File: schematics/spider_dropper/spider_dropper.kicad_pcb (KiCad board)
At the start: 2 copper layers, 80 x 20 mm, 10 parts, among them J1 JST_XH_3, J2 PJ-044AH, J3 JST_XH_2, Q1 IRLZ34N, SW1 ZX40E20C01

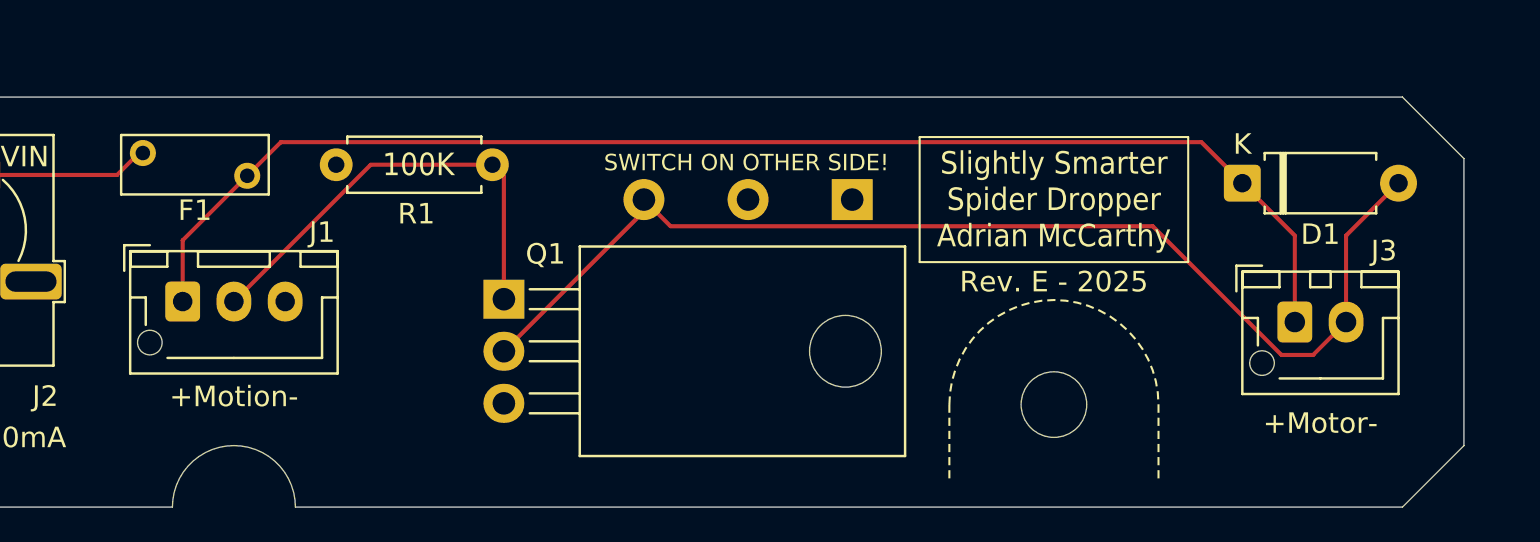
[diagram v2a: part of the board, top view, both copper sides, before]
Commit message: Small improvements for Rev. E.
* Moved the connectors to make it easier to connect & disconnect.
* Moved the diode in from the corner.
* Added detail to the perimeter boundary (in User Drawings layer).
* Added a triangular arrow to assist with alignment in assembly.
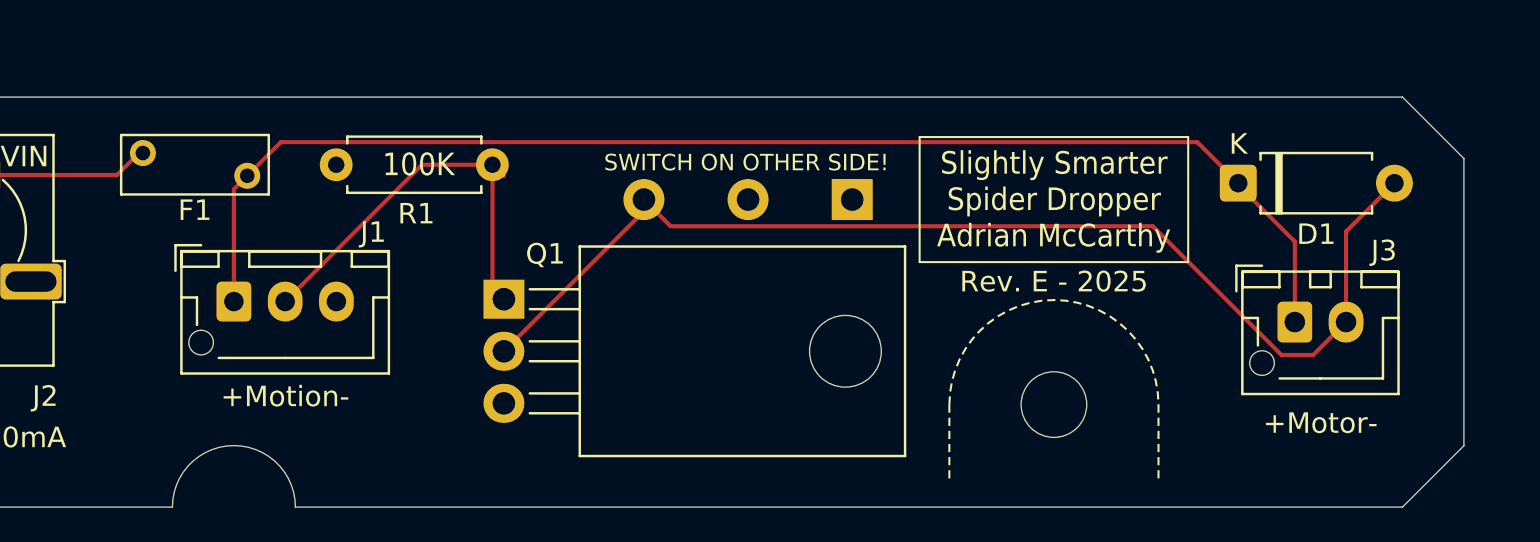
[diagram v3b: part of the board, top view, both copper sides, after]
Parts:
- moved J1 2.50 mm to (129.9, 108.3)
- moved D1 0.20 mm to (178.9, 102.5)
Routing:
- net /MOTION: track 22.2 -> 20.5 mm
- net /MOTOR+: track 65.3 -> 64.2 mm
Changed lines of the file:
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@@
 	(title_block
 		(title "Slightly Smarter Simple Spider Dropper")
-		(date "2025-08-28")
+		(date "2025-09-18")
 		(rev "E")
 		(company "Adrian McCarthy")
@@
 		(comment 6 "corrected footprint for power connector")
 		(comment 7 "nudged diode away from corner")
+		(comment 8 "added arrow on b. silkscreen")
 	)
 	(layers
@@
 	(footprint "Diode_THT:D_A-405_P7.62mm_Horizontal"
 		(layer "F.Cu")
-		(at 179.09 102.5)
+		(at 178.89 102.5)
 		(descr "Diode, A-405 series, Axial, Horizontal, pin pitch=7.62mm, length*diameter=5.2*2.7mm^2, http://www.diodes.com/_files/packages/A-405.pdf")
 		(tags "Diode A-405 series Axial Horizontal pin pitch 7.62mm  length 5.2mm diameter 2.7mm")
@@
 	(footprint "Connector_JST:JST_XH_B3B-XH-AM_1x03_P2.50mm_Vertical"
 		(layer "F.Cu")
-		(at 127.4 108.275)
+		(at 129.9 108.275)
 		(descr "JST XH series connector, B3B-XH-AM, with boss (http://www.jst-mfg.com/product/pdf/eng/eXH.pdf), generated with kicad-footprint-generator")
 		(tags "connector JST XH vertical boss")
@@
 		(layer "F.SilkS")
 	)
+	(gr_poly
+		(pts
+			(xy 111.2 108.3) (xy 113 107.4) (xy 113 109.2)
+		)
+		(stroke
+			(width 0.1)
+			(type solid)
+		)
+		(fill yes)
+		(layer "B.SilkS")
+	)
 	(gr_circle
 		(center 169.9 113.3)
@@
 		(layer "Dwgs.User")
 	)
+	(gr_arc
+		(start 125.8 117.1)
+		(mid 129.9 114.027998)
+		(end 134 117.1)
+		(stroke
+			(width 0.1)
+			(type default)
+		)
+		(layer "Dwgs.User")
+	)
+	(gr_line
+		(start 188.7 114.8)
+		(end 186.4 117.1)
+		(stroke
+			(width 0.1)
+			(type default)
+		)
+		(layer "Dwgs.User")
+	)
+	(gr_line
+		(start 125.8 117.1)
+		(end 111.1 117.1)
+		(stroke
+			(width 0.1)
+			(type default)
+		)
+		(layer "Dwgs.User")
+	)
 	(gr_line
 		(start 215.7 108.3)
@@
 	)
 	(gr_line
+		(start 186.4 99.5)
+		(end 188.7 101.8)
+		(stroke
+			(width 0.1)
+			(type default)
+		)
+		(layer "Dwgs.User")
+	)
+	(gr_line
+		(start 186.4 117.1)
+		(end 133.999999 117.1)
+		(stroke
+			(width 0.1)
+			(type default)
+		)
+		(layer "Dwgs.User")
+	)
+	(gr_line
 		(start 149.9 97.8)
 		(end 149.9 105.8)
@@
 		(layer "Dwgs.User")
 	)
-	(gr_rect
+	(gr_line
+		(start 188.7 101.8)
+		(end 188.7 114.8)
+		(stroke
+			(width 0.1)
+			(type default)
+		)
+		(layer "Dwgs.User")
+	)
+	(gr_line
 		(start 111.1 99.5)
-		(end 188.7 117.1)
+		(end 186.4 99.5)
+		(stroke
+			(width 0.1)
+			(type default)
+		)
+		(layer "Dwgs.User")
+	)
+	(gr_line
+		(start 111.1 117.1)
+		(end 111.1 99.5)
 		(stroke
 			(width 0.1)
 			(type default)
 		)
-		(fill no)
 		(layer "Dwgs.User")
 	)
@@
 	)
 	(gr_text "+Motion-"
-		(at 129.9 113.5 0)
+		(at 132.4 113.5 0)
 		(layer "F.SilkS")
 		(effects
@@
 	)
 	(segment
-		(start 127.4 108.275)
-		(end 127.4 105.29)
+		(start 178.89 102.59)
+		(end 181.65 105.35)
 		(width 0.2)
 		(layer "F.Cu")
@@
 	)
 	(segment
-		(start 181.65 105.06)
-		(end 179.09 102.5)
+		(start 181.65 105.35)
+		(end 181.65 109.275)
 		(width 0.2)
 		(layer "F.Cu")
@@
 	)
 	(segment
-		(start 181.65 109.275)
-		(end 181.65 105.06)
+		(start 132.191 100.499)
+		(end 176.889 100.499)
 		(width 0.2)
 		(layer "F.Cu")
@@
 	)
 	(segment
-		(start 177.089 100.499)
+		(start 130.55 102.14)
 		(end 132.191 100.499)
 		(width 0.2)
@@
 	)
 	(segment
-		(start 179.09 102.5)
-		(end 177.089 100.499)
+		(start 178.89 102.5)
+		(end 178.89 102.59)
 		(width 0.2)
 		(layer "F.Cu")
@@
 	)
 	(segment
-		(start 127.4 105.29)
-		(end 130.55 102.14)
+		(start 129.9 108.275)
+		(end 129.9 102.79)
 		(width 0.2)
 		(layer "F.Cu")
@@
 	)
 	(segment
-		(start 132.191 100.499)
+		(start 129.9 102.79)
 		(end 130.55 102.14)
 		(width 0.2)
@@
 	)
 	(segment
-		(start 186.71 102.5)
-		(end 184.15 105.06)
+		(start 176.889 100.499)
+		(end 178.89 102.5)
 		(width 0.2)
 		(layer "F.Cu")
-		(net 5)
+		(net 4)
 	)
 	(segment
@@
 	)
 	(segment
-		(start 184.15 105.06)
+		(start 184.15 104.86)
 		(end 184.15 109.275)
 		(width 0.2)
@@
 	)
 	(segment
-		(start 136.575 101.6)
-		(end 142.51 101.6)
+		(start 186.51 102.5)
+		(end 184.15 104.86)
+		(width 0.2)
+		(layer "F.Cu")
+		(net 5)
+	)
+	(segment
+		(start 132.4 108.275)
+		(end 139.075 101.6)
 		(width 0.2)
 		(layer "F.Cu")
@@
 	)
 	(segment
-		(start 143.07 108.16)
-		(end 143.07 102.16)
+		(start 142.51 107.6)
+		(end 143.07 108.16)
+		(width 0.2)
+		(layer "F.Cu")
+		(net 6)
+	)
+	(segment
+		(start 139.075 101.6)
+		(end 142.51 101.6)
 		(width 0.2)
 		(layer "F.Cu")
@@
 	)
 	(segment
-		(start 129.9 108.275)
-		(end 136.575 101.6)
+		(start 142.51 101.6)
+		(end 142.51 107.6)
 		(width 0.2)
 		(layer "F.Cu")
@@
 		)
 	)
+	(group ""
+		(members "1a110cda-c5c4-4d6f-9856-7c3907b5bba1" "1ba40044-9f59-4987-8364-2ef93bba9d79"
+			"79ad52df-f96e-4c85-854d-0dd0dc49f08a" "cd2ad88d-1473-40dd-a4fc-b80dc6a883e4"
+			"d2219a55-52e0-4438-a1ba-f4ec083b581e" "e5993648-c71e-4bc1-9e7f-92ee8b79d6de"
+			"fc64db34-372b-49d4-b4d6-4ea789881956" "fe8aa7d5-6fb3-46ed-a818-365fcd90bb6e"
+		)
+	)

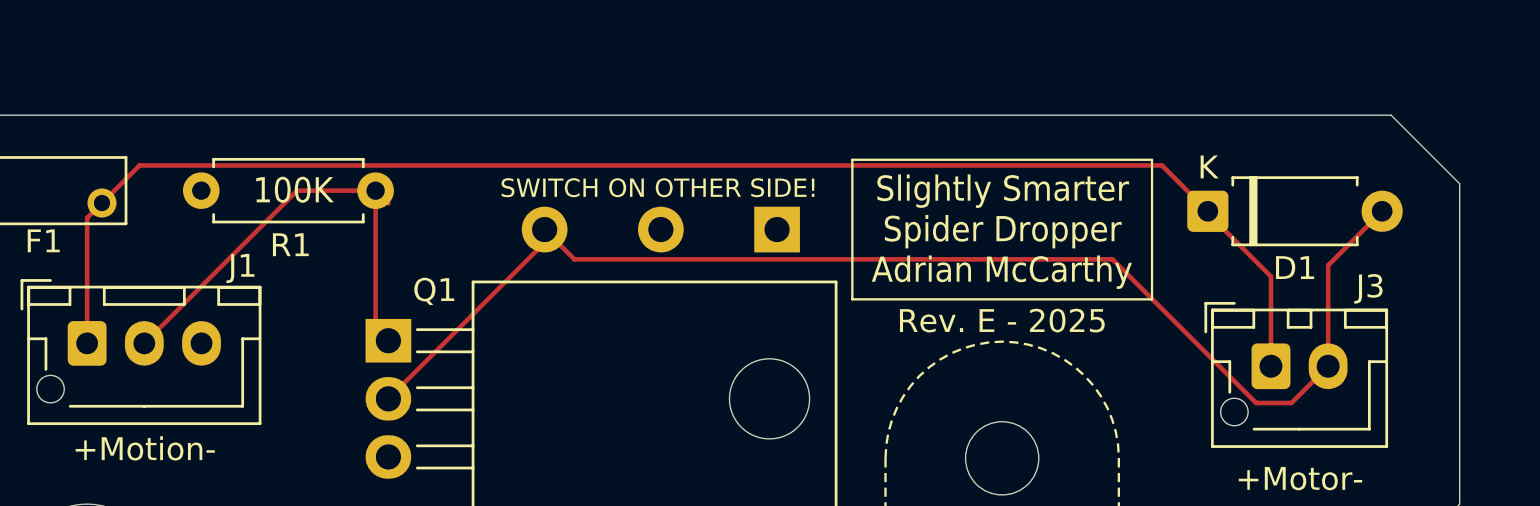
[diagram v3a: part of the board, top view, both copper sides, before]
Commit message: Changed the diode footprint to a DO-41.
The leads of the 1N4001 diodes I have barely fit into the holes for the
default footprint.  Datasheet suggests DO-41 is the correct package,
and KiCad has a footprint for that with the same spacing but larger
holes.
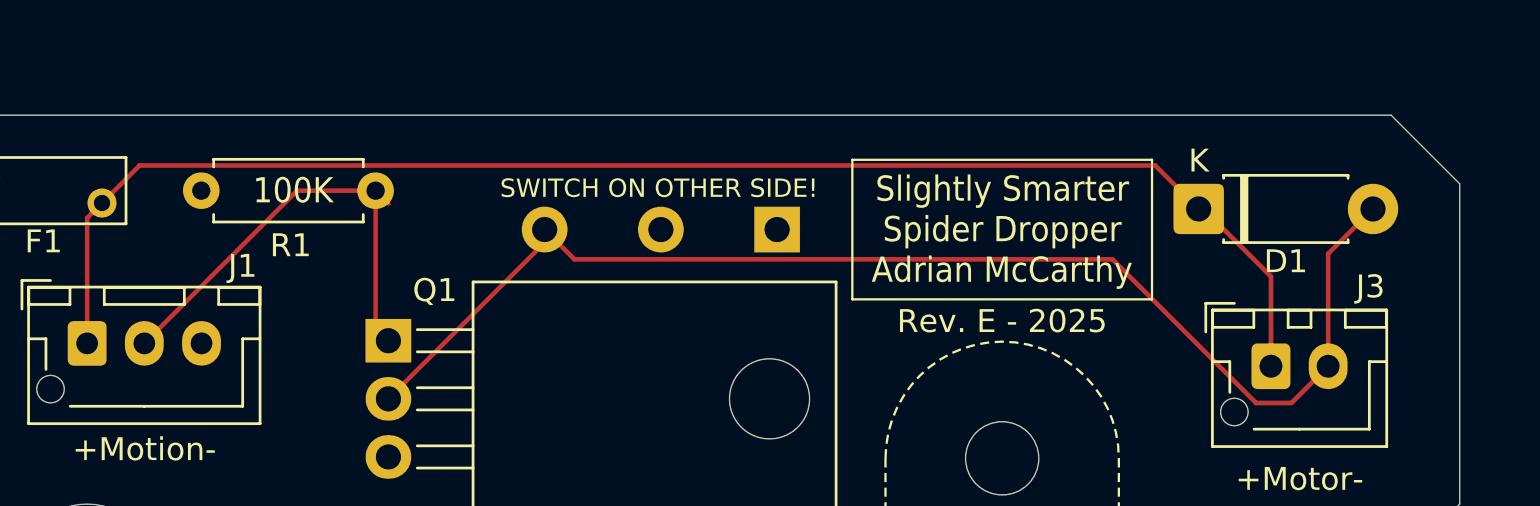
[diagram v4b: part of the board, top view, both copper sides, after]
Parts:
- D1: footprint Diode_THT:D_A-405_P7.62mm_Horizontal -> Diode_THT:D_DO-41_SOD81_P7.62mm_Horizontal
- moved D1 0.41 mm to (178.5, 102.4)
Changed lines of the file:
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@@
 	(title_block
 		(title "Slightly Smarter Simple Spider Dropper")
-		(date "2025-09-18")
+		(date "2025-09-21")
 		(rev "E")
 		(company "Adrian McCarthy")
@@
 	(net 6 "/MOTION")
 	(net 7 "unconnected-(J2-Pad3)")
-	(footprint "Diode_THT:D_A-405_P7.62mm_Horizontal"
+	(footprint "Diode_THT:D_DO-41_SOD81_P7.62mm_Horizontal"
 		(layer "F.Cu")
-		(at 178.89 102.5)
-		(descr "Diode, A-405 series, Axial, Horizontal, pin pitch=7.62mm, length*diameter=5.2*2.7mm^2, http://www.diodes.com/_files/packages/A-405.pdf")
-		(tags "Diode A-405 series Axial Horizontal pin pitch 7.62mm  length 5.2mm diameter 2.7mm")
+		(at 178.49 102.4)
+		(descr "Diode, DO-41_SOD81 series, Axial, Horizontal, pin pitch=7.62mm, length*diameter=5.2*2.7mm^2, https://www.diodes.com/assets/Package-Files/DO-41-Plastic.pdf")
+		(tags "Diode DO-41_SOD81 series Axial Horizontal pin pitch 7.62mm  length 5.2mm diameter 2.7mm")
 		(property "Reference" "D1"
-			(at 3.81 2.5 0)
+			(at 3.81 2.3 0)
 			(layer "F.SilkS")
 			(effects
@@
 		(property "Datasheet" "~"
 			(at 0 0 0)
-			(unlocked yes)
 			(layer "F.Fab")
 			(hide yes)
@@
 		(property "Description" "Diode"
 			(at 0 0 0)
-			(unlocked yes)
 			(layer "F.Fab")
 			(hide yes)
@@
 		)
 		(fp_line
-			(start 1.09 -1.14)
+			(start 1.09 -1.34)
 			(end 1.09 -1.47)
 			(stroke
@@
 		)
 		(fp_line
-			(start 1.09 1.14)
+			(start 1.09 1.34)
 			(end 1.09 1.47)
 			(stroke
@@
 		(fp_line
 			(start 6.53 -1.47)
-			(end 6.53 -1.14)
+			(end 6.53 -1.34)
 			(stroke
 				(width 0.12)
@@
 		(fp_line
 			(start 6.53 1.47)
-			(end 6.53 1.14)
+			(end 6.53 1.34)
 			(stroke
 				(width 0.12)
@@
 		)
 		(fp_rect
-			(start -1.15 -1.6)
-			(end 8.77 1.6)
+			(start -1.35 -1.6)
+			(end 8.97 1.6)
 			(stroke
 				(width 0.05)
@@
 		)
 		(fp_text user "K"
-			(at 0 -1.9 0)
+			(at 0 -2.1 0)
 			(layer "F.SilkS")
 			(effects
@@
 		)
 		(fp_text user "K"
-			(at 0 -1.9 0)
+			(at 0 -2.1 0)
 			(layer "F.Fab")
 			(effects
@@
 		(pad "1" thru_hole roundrect
 			(at 0 0)
-			(size 1.8 1.8)
-			(drill 0.9)
+			(size 2.2 2.2)
+			(drill 1.1)
 			(layers "*.Cu" "*.Mask")
 			(remove_unused_layers no)
-			(roundrect_rratio 0.138889)
+			(roundrect_rratio 0.113636)
 			(net 4 "/MOTOR+")
 			(pinfunction "K")
@@
 		(pad "2" thru_hole circle
 			(at 7.62 0)
-			(size 1.8 1.8)
-			(drill 0.9)
+			(size 2.2 2.2)
+			(drill 1.1)
 			(layers "*.Cu" "*.Mask")
 			(remove_unused_layers no)
@@
 		)
 		(embedded_fonts no)
-		(model "${KICAD9_3DMODEL_DIR}/Diode_THT.3dshapes/D_A-405_P7.62mm_Horizontal.step"
+		(model "${KICAD9_3DMODEL_DIR}/Diode_THT.3dshapes/D_DO-41_SOD81_P7.62mm_Horizontal.step"
 			(offset
 				(xyz 0 0 0)
@@
 	)
 	(segment
-		(start 178.89 102.59)
-		(end 181.65 105.35)
+		(start 132.191 100.499)
+		(end 176.589 100.499)
 		(width 0.2)
 		(layer "F.Cu")
@@
 	)
 	(segment
-		(start 132.191 100.499)
-		(end 176.889 100.499)
+		(start 181.65 105.35)
+		(end 178.7 102.4)
+		(width 0.2)
+		(layer "F.Cu")
+		(net 4)
+	)
+	(segment
+		(start 178.7 102.4)
+		(end 178.49 102.4)
 		(width 0.2)
 		(layer "F.Cu")
@@
 	)
 	(segment
-		(start 176.889 100.499)
-		(end 178.89 102.5)
+		(start 176.589 100.499)
+		(end 178.49 102.4)
 		(width 0.2)
 		(layer "F.Cu")
@@
 	)
 	(segment
-		(start 184.15 104.86)
-		(end 184.15 109.275)
+		(start 184.15 104.36)
+		(end 186.11 102.4)
 		(width 0.2)
 		(layer "F.Cu")
@@
 	(segment
 		(start 184.15 109.275)
-		(end 182.543917 110.881083)
+		(end 184.15 104.36)
 		(width 0.2)
 		(layer "F.Cu")
@@
 	)
 	(segment
-		(start 149.9 103.87)
-		(end 149.9 103.3)
+		(start 184.15 109.275)
+		(end 182.543917 110.881083)
 		(width 0.2)
 		(layer "F.Cu")
@@
 	)
 	(segment
-		(start 186.51 102.5)
-		(end 184.15 104.86)
+		(start 149.9 103.87)
+		(end 149.9 103.3)
 		(width 0.2)
 		(layer "F.Cu")
